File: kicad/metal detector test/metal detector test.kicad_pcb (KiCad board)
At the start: 4 copper layers, 82.8 x 88.9 mm, 110 parts, among them J1 3.5mm audio jack TRS, Q1 PNP, Q2 NPN, SW0 SW_SPST, SW1 SW_SPST, SW10 SW_SPST, SW2 SW_SPST, SW3 SW_SPST, SW4 SW_SPST, SW5 SW_SPST, SW6 SW_SPST, SW7 SW_SPST, SW8 SW_SPST, U1 op amp (higher voltage), U10 3.3v lin reg, U11 lp filter, U12 op amp (lower voltage), U2 nucleo-32 uC module, U3 9v lin reg, U4 5v lin reg, U5 3.3v lin reg, U6 audio amp, U7 lp filter, U8 switch debounce, U9 5v lin reg

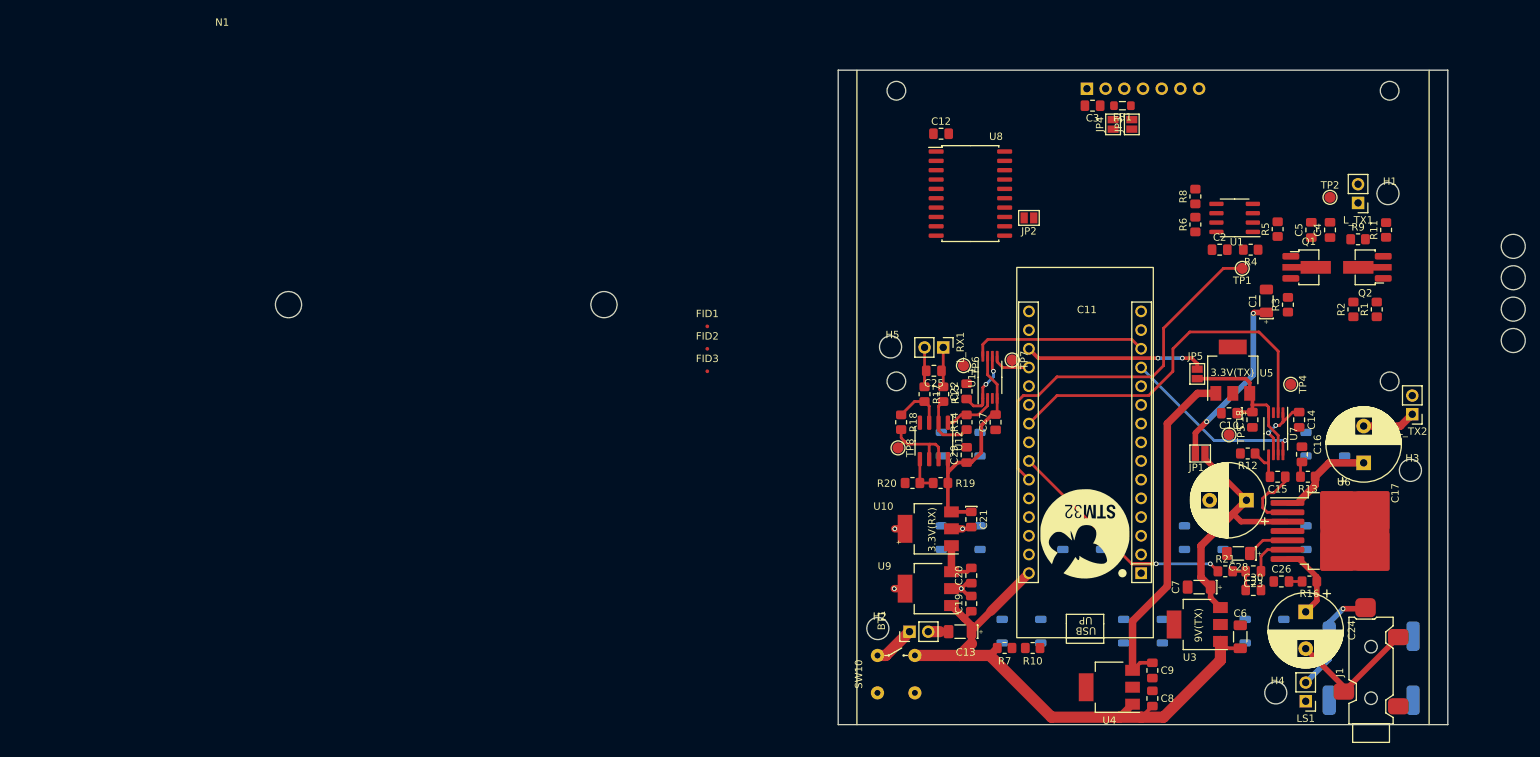
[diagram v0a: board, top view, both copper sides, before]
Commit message: Everything but gnd should be routed
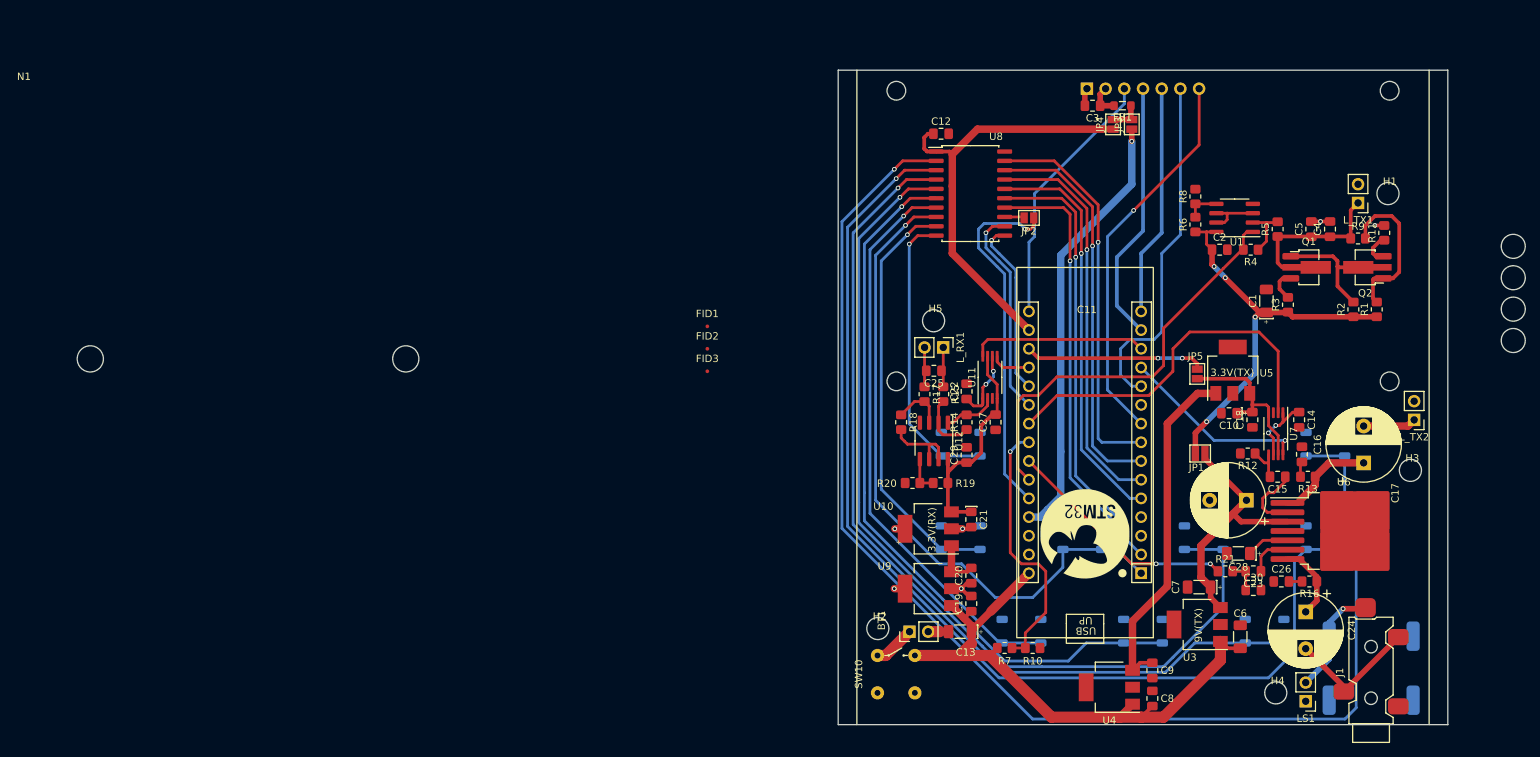
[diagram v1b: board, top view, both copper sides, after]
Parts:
- removed TP1: TX_A_SCALED, TestPoint:TestPoint_Pad_D1.5mm
- removed TP2: TX_A_RAW, TestPoint:TestPoint_Pad_D1.5mm
- removed TP4: TX_D_RAW, TestPoint:TestPoint_Pad_D1.5mm
- removed TP5: TX_D_FILT, TestPoint:TestPoint_Pad_D1.5mm
- removed TP6: RX_RAW, TestPoint:TestPoint_Pad_D1.5mm
- removed TP7: RX_FILT, TestPoint:TestPoint_Pad_D1.5mm
- removed TP8: 1.6v, TestPoint:TestPoint_Pad_D1.5mm
- moved N1 27.9 mm to (-110.6, 1.37)
- moved SW2 15.1 mm to (57.9, 76.2)
- moved SW3 15.1 mm to (49.7, 63.5)
- moved H5 6.84 mm to (13.0, 34.0)
- moved L_TX2 0.80 mm to (78.2, 47.5)
- moved R11 0.47 mm to (74.2, 22.1)
- moved C4 0.11 mm to (66.8, 21.6)
- moved C5 0.11 mm to (64.3, 21.6)
- moved R9 0.11 mm to (70.6, 22.9)
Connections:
- U2 pad 11: Net-(DS1-RES) -> Net-(DS1-DC)
- U2 pad 15: Net-(DS1-DC) -> Net-(DS1-RES)
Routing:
- net Net-(SW0-B): track 0.00 -> 179.2 mm, vias 0 -> 1
- net Net-(SW1-B): track 0.00 -> 146.4 mm, vias 0 -> 1
- net Net-(SW3-B): track 0.00 -> 125.9 mm, vias 0 -> 1
- net Net-(SW2-B): track 0.00 -> 122.4 mm, vias 0 -> 1
- net Net-(SW4-B): track 0.00 -> 99.3 mm, vias 0 -> 1
- net Net-(SW6-B): track 0.00 -> 83.9 mm, vias 0 -> 1
- net Net-(SW5-B): track 0.00 -> 77.7 mm, vias 0 -> 1
- net SW5: track 0.00 -> 62.0 mm, vias 0 -> 1
- net SW4: track 0.00 -> 60.6 mm, vias 0 -> 1
- net Net-(JP3-A): track 0.00 -> 59.4 mm, vias 0 -> 1
- net +3.3V_uC: track 0.00 -> 58.6 mm
- net Net-(SW7-B): track 0.00 -> 57.2 mm, vias 0 -> 1
- net SW3: track 0.00 -> 55.0 mm, vias 0 -> 1
- net SW2: track 0.00 -> 54.5 mm, vias 0 -> 1
- net SW1: track 0.00 -> 53.9 mm, vias 0 -> 1
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
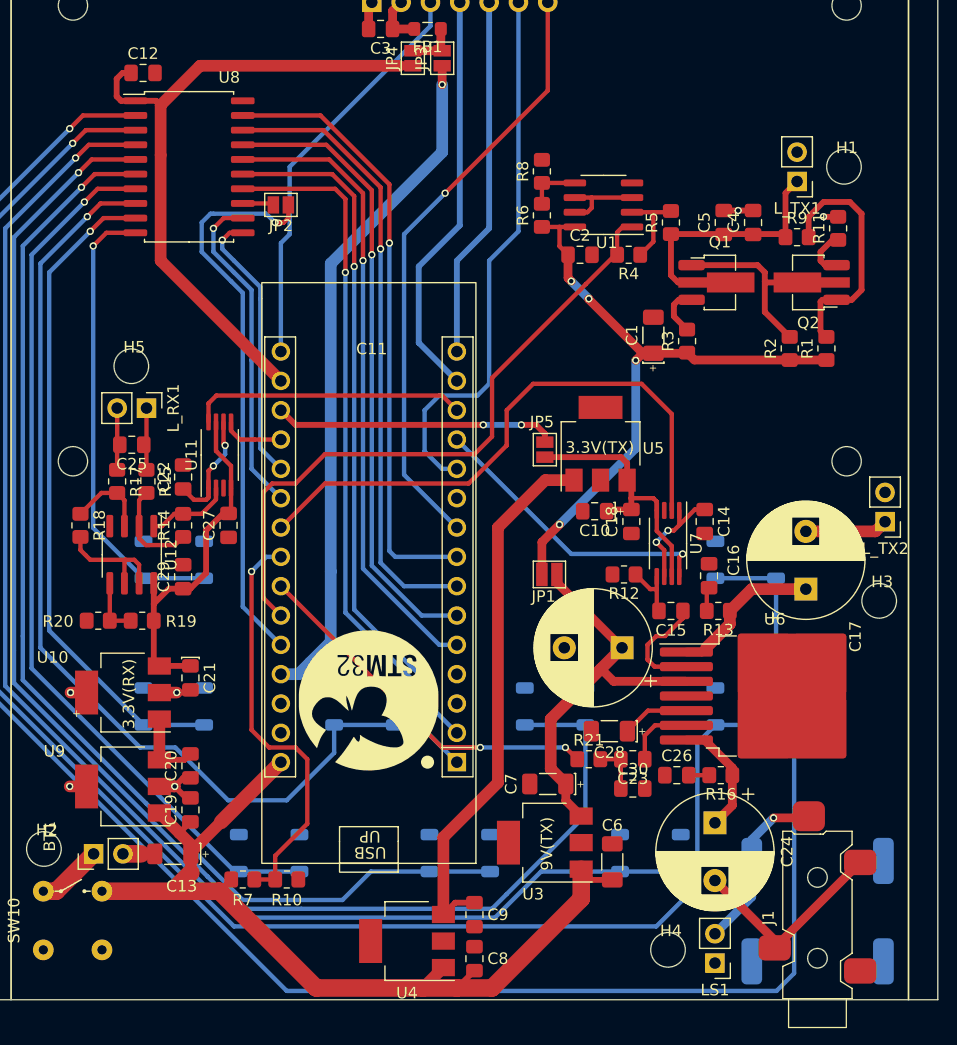
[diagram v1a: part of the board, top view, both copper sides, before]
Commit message: Finished routing I think, needs testing.  Need to position designators as well.
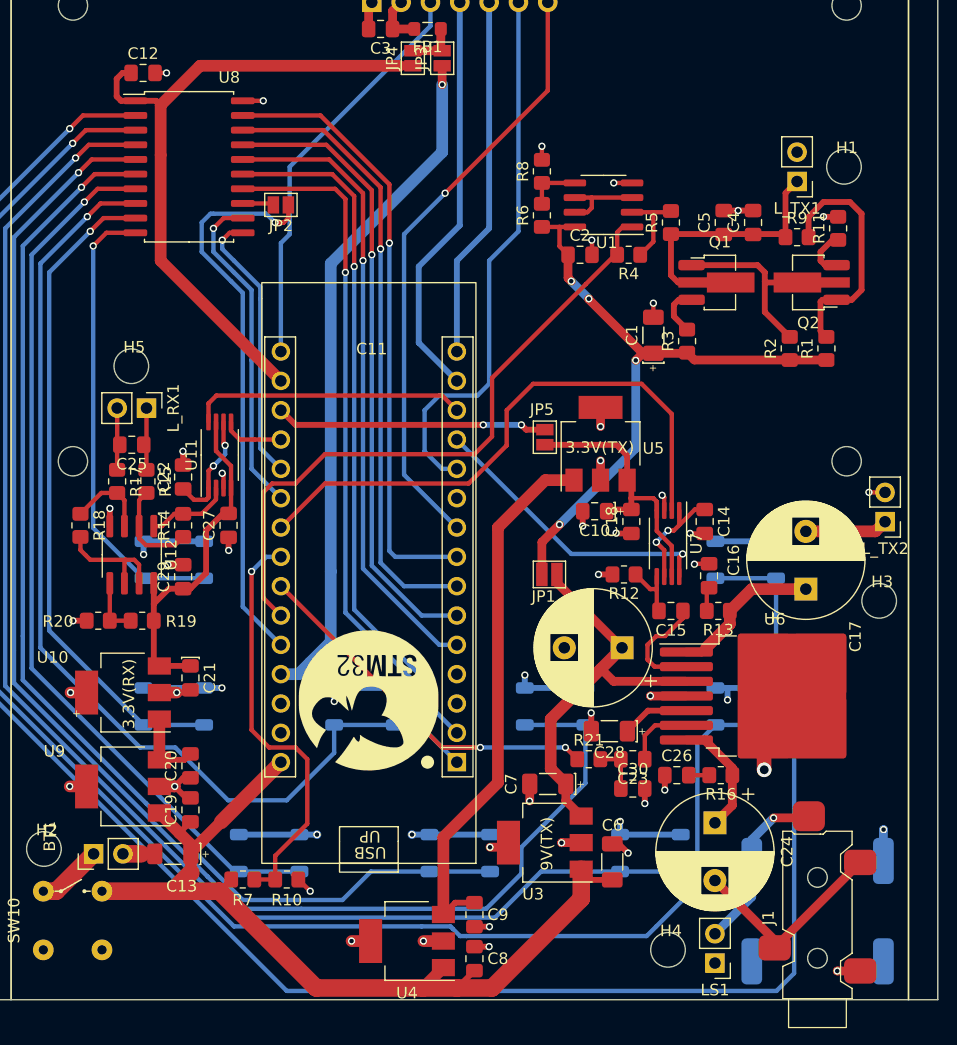
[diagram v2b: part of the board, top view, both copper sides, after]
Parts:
- moved JP5 1.08 mm to (48.8, 40.2)
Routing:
- net GNDA: track 19.4 -> 136.0 mm, vias 6 -> 52
- net Net-(JP5-A): track 24.4 -> 23.6 mm
- net +3.3VA: track 23.1 -> 23.9 mm
- net Net-(SW1-B): track 146.4 -> 147.1 mm
- added copper zone on In1.Cu, net GNDA
- added copper zone on In2.Cu, net GNDA

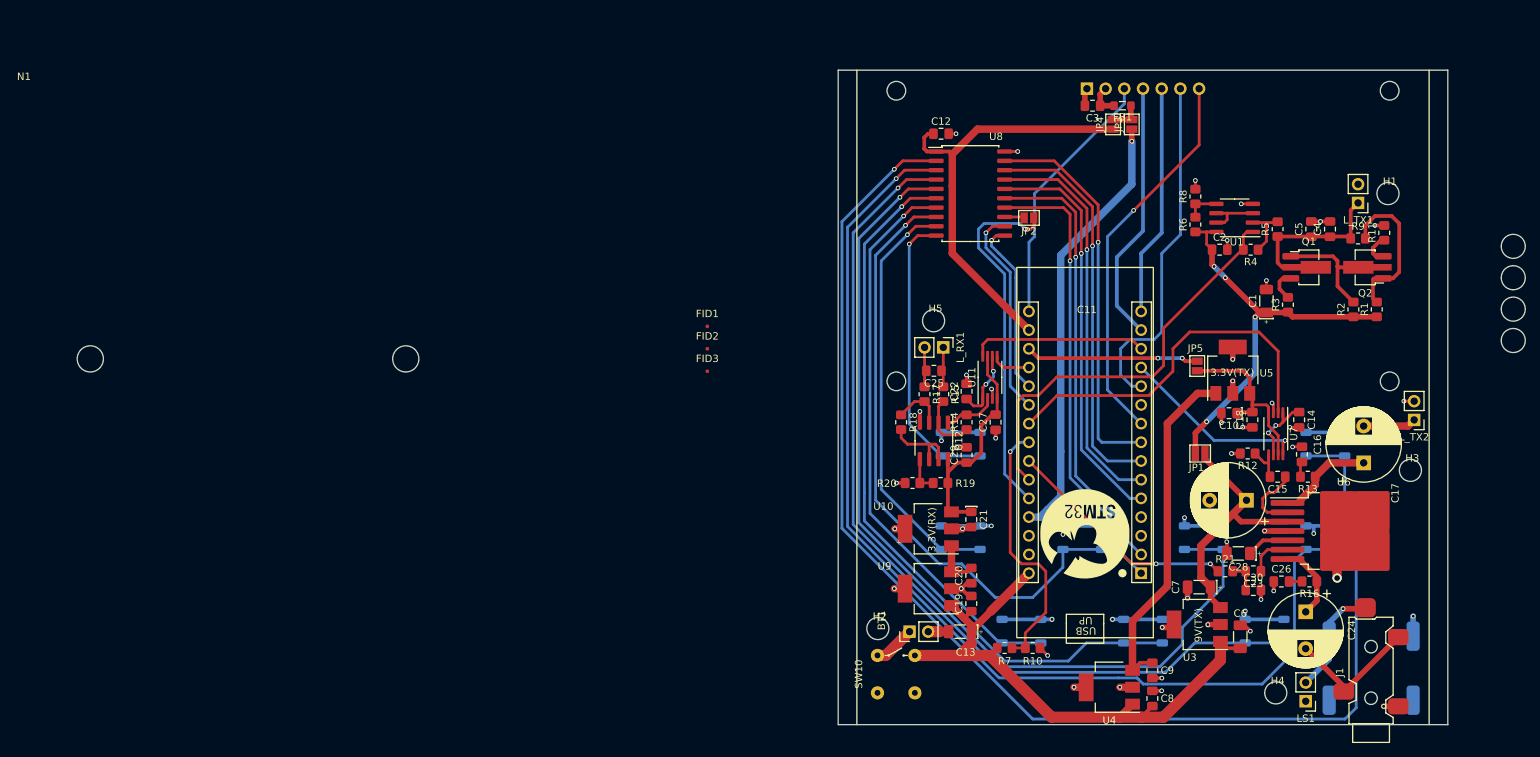
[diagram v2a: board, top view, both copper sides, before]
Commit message: via stitching, designator placement
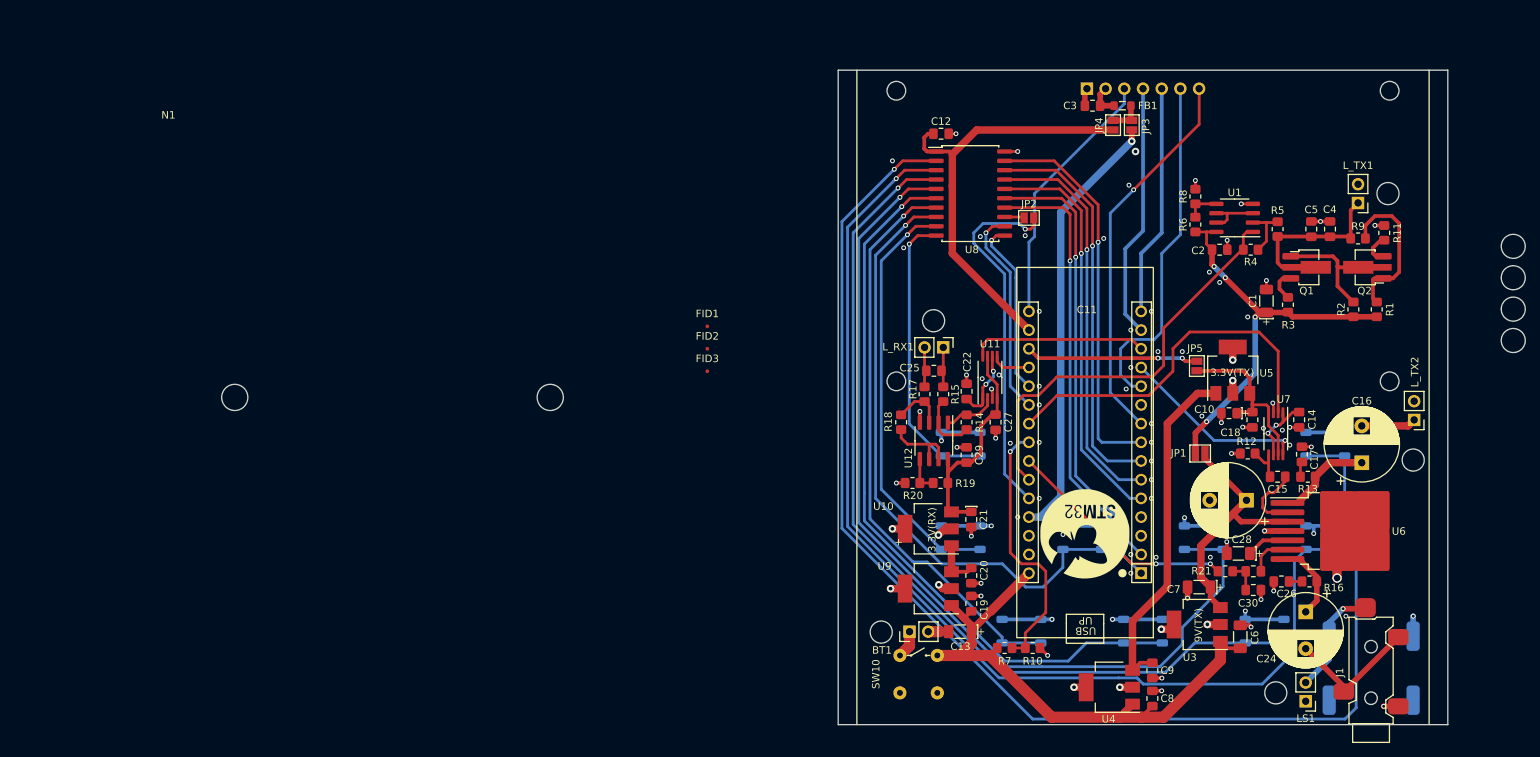
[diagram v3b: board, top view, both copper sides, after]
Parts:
- moved N1 20.3 mm to (-91.0, 6.60)
- moved SW10 3.05 mm to (8.38, 79.5)
- moved H3 1.45 mm to (78.1, 53.0)
- moved H2 0.66 mm to (5.84, 76.3)
- moved C16 0.25 mm to (71.1, 53.3)
- moved JP3 0.10 mm to (39.9, 7.47)
- moved JP4 0.10 mm to (37.3, 7.47)
- moved JP5 0.05 mm to (48.7, 40.2)
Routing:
- net +BATT: track 81.0 -> 78.0 mm
- net AUDIO: track 34.4 -> 31.9 mm
- net Net-(BT1-+): track 5.69 -> 3.77 mm
- net GNDA: track 136.0 -> 137.4 mm, vias 52 -> 93
- net Net-(SW6-B): track 83.9 -> 82.6 mm
- net Net-(DS1-SDA): track 35.6 -> 34.7 mm
- net Net-(SW5-B): track 77.7 -> 78.6 mm
- net /(BACKCH_TX): track 48.8 -> 49.4 mm

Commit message: Added a lot of fun silkscreen logos, and some other small tweaks
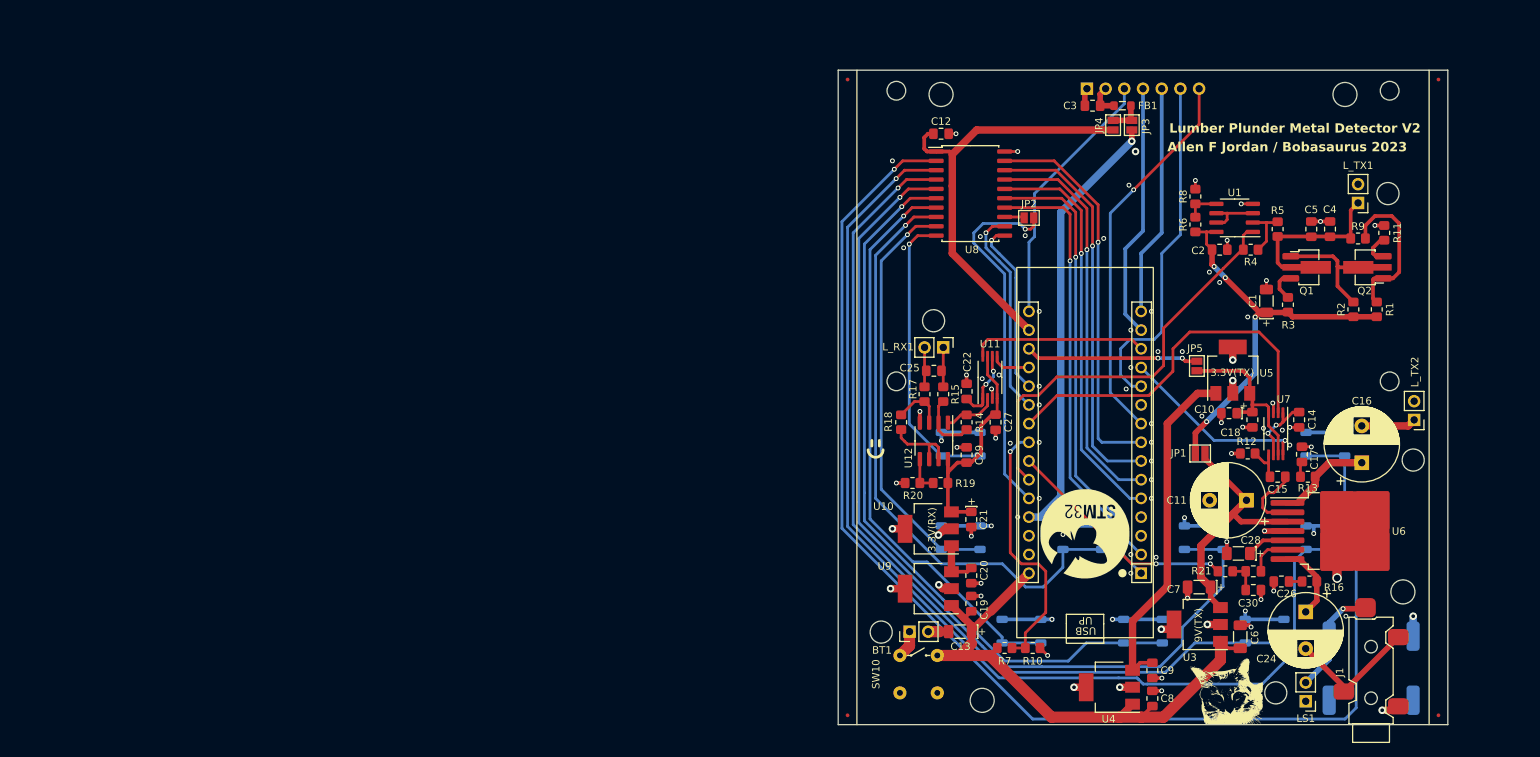
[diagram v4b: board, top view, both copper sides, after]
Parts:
- removed N1: battery holder, allen footprints:106990288_18650_x3_battery_holder
- added FID4: Fiducial, Fiducial:Fiducial_0.5mm_Mask1.5mm, F.Cu at (81.5, 87.6)
- added G***: LOGO, LOGO, F.Cu at (52.7, 84.3)
- added G***: LOGO, LOGO, B.Cu at (75.4, 60.9)
- added G***: LOGO, LOGO, B.Cu at (7.64, 60.9)
- added G***: LOGO, LOGO, B.Cu at (62.5, 30.7)
- moved FID2 105.8 mm to (81.5, 1.27)
- moved bobasaurus_logo 102.5 mm to (22.1, 15.2)
- moved H9 87.1 mm to (19.6, 85.6)
- moved H8 83.0 mm to (14.0, 3.30)
- moved FID3 50.5 mm to (1.27, 87.6)
- moved H6 49.3 mm to (76.7, 70.9)
- moved FID1 38.6 mm to (1.27, 1.27)
- moved H7 33.8 mm to (68.8, 3.30)
- renumbered G*** to bobasaurus_logo
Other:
- board text added: "Allen F Jordan / Bobasaurus 2023"
- board text added: "Lumber Plunder Metal Detector V2"

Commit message: Should be ready for fabrication
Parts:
- added ?: , , F.Cu at (4.06, 87.4)
- added ?: , , F.Cu at (4.06, 1.52)
- added C31: 3.3u, allen footprints:C_Polarized_0805_2012Metric_HandSolder_allen, F.Cu at (34.2, 6.86)
- added JP6: SolderJumper_2_Open, Jumper:SolderJumper-2_P1.3mm_Open_Pad1.0x1.5mm, B.Cu at (29.0, 59.3)
- G***: moved to B.Cu
- moved G*** 62.5 mm to (20.4, 30.7), turned to 180 degrees
- moved bobasaurus_logo 19.1 mm to (41.1, 15.6)
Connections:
- U2 pad 27: Net-(JP3-A) -> Net-(JP6-A)
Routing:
- net Net-(JP3-A): track 59.4 -> 55.2 mm
- net Net-(JP6-A): track 0.00 -> 2.98 mm
- net Net-(DS1-VCC): track 4.49 -> 6.68 mm
- net GNDA: track 137.9 -> 139.0 mm, vias 93 -> 94
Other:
- board text added: "4-40"
- board text added: "GND"
- board text added: "SR"
